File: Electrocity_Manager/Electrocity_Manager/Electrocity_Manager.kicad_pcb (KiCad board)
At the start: 2 copper layers, 100 x 77 mm, 193 parts, among them IC2 MAIN_SHUTDOWN, IC3 RELAY_STATE, IC4 ADC_RST, J1 SERIAL, P1 SWD, P10 EMERGENCY, P11 EMERGENCY, P12 FRAME_GRAND, P13 BATT_IN, P14 POWER_OUT, P15 FUN_OUT, P16 BATT_IN, P17 POWER_OUT, P18 FUN_OUT, P2 CAN, P3 CAN, P4 EMERGENCY_SIGNAL, P5 EMERGENCY_SIGNAL, P6 12V_OUT, P7 12V_OUT, P9 MAIN_SW, Q1 FET_N, Q2 NPN, Q3 NPN, Q4 NPN, Q5 NPN, Q6 NPN, Q7 FET_N, SW1 RST, U1 MAX3051, U10 BD9G101G, U11 ACS781, U12 V23134J1052D642, U13 ACS70331, U14 ACS781, U15 BD33FA1, U16 EC12PLRGBSDVBF, U17 LOGO, U18 LOGO, U19 MCP2221A, U2 STM32F405RG, U20 OSRB38C9AA, U21 OSRB38C9AA, U22 HSIN_946, U3 FULLCOLOR, U4 AQM0802_BL, U5 AP3211, U6 SI8900, U7 AZ1086H, U8 V23134J1052D642, U9 RPA60-12FW/P, X1 8MHz

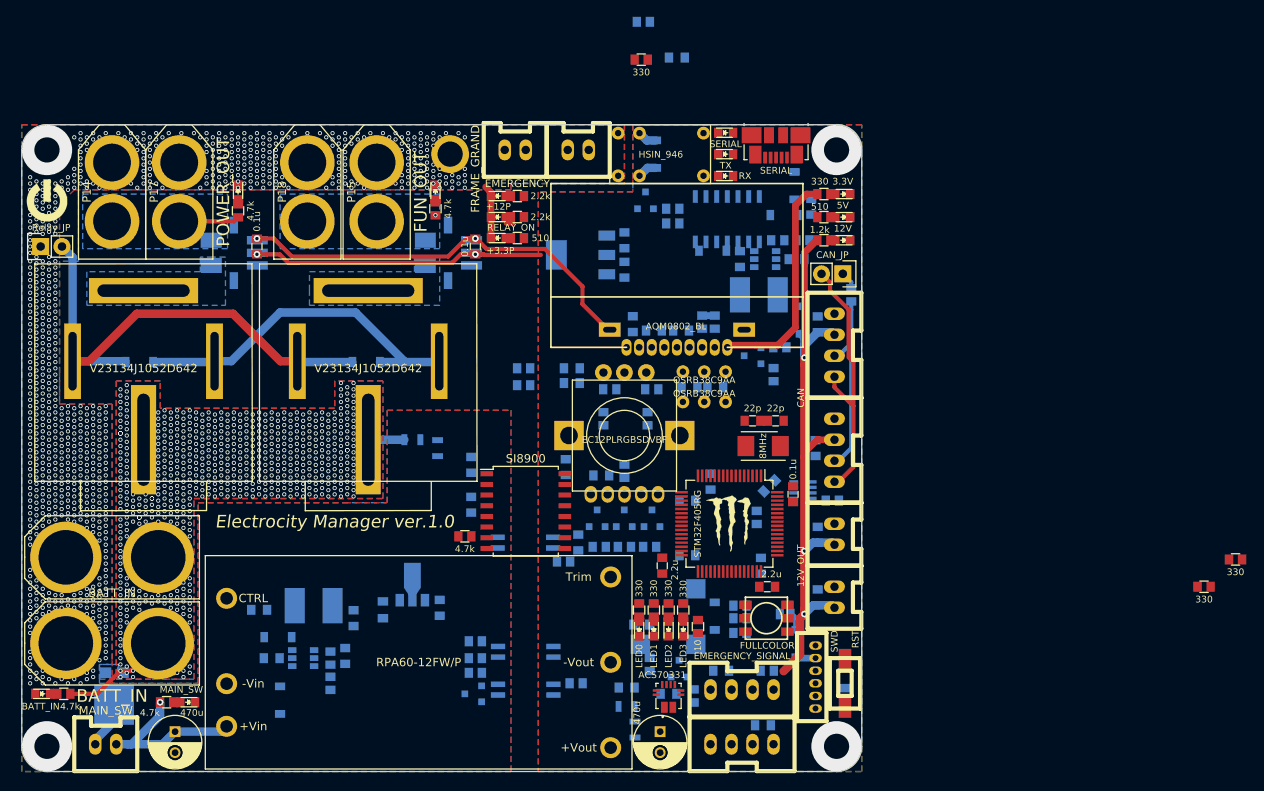
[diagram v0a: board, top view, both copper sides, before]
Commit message: 電源配線完了.フルカラーの秋月のエンコーダ基板面積的に使用できなかった...
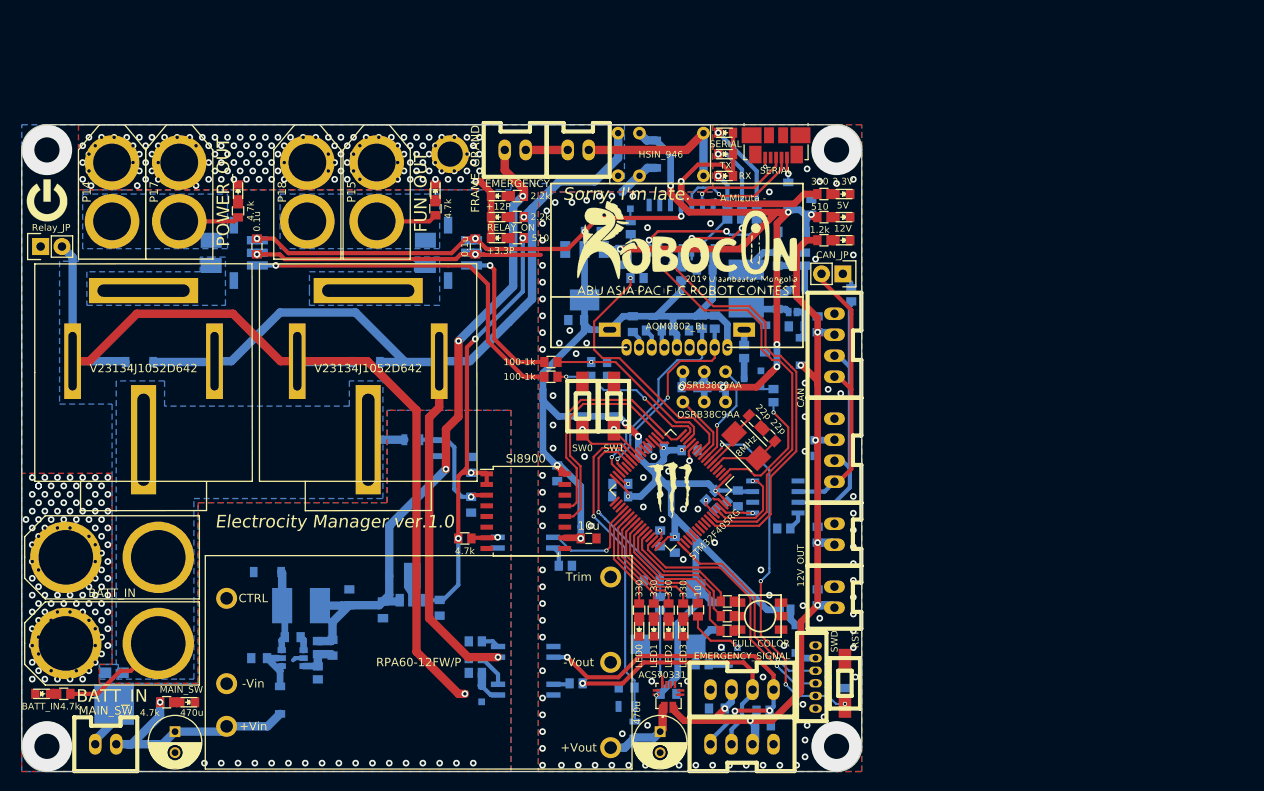
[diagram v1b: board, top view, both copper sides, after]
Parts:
- removed C45: 0.1u, Mizz_lib:C_0603
- removed Q4, Q5, Q6: NPN, Mizz_lib:SOT-123
- removed R49: 510, Mizz_lib:R_0603
- removed R50, R54, R55: 10k, Mizz_lib:R_0603
- removed R56, R57: 100, Mizz_lib:R_0603
- added C49: 10u, Mizz_lib:C_0603, B.Cu at (116.0, 110.8)
- added SW2: SW0, Mizz_lib:SW_SPST_CK_RS282G05A3, F.Cu at (114.8, 131.5)
- added SW3: SW1, Mizz_lib:SW_SPST_CK_RS282G05A3, F.Cu at (118.5, 131.5)
- added U23: LOGO, Mizz_lib:Battery_Killer_logo, B.Cu at (58.5, 154.5)
- C11, C13, C4, R19, R51, R58: moved to B.Cu
- C24, C26: value 22u -> 10u
- C28, R21, R40, R44: moved to F.Cu
- R1, R5: value 510 -> 330; moved to F.Cu
- R22, R23: value 330 -> 10k
- U1: footprint Package_TO_SOT_SMD:SOT-23-8 -> Mizz_lib:SOIC-8_3.9x4.9mm_Pitch1.27mm
- U16: value EC12PLRGBSDVBF -> LOGO; footprint Mizz_lib:EC12PLRGBSDVBF -> Mizz_lib:Robocon2019_30.0x30.0_silk
- U2: footprint Housings_QFP:TQFP-64_10x10mm_Pitch0.5mm -> Package_QFP:LQFP-64_10x10mm_P0.5mm
- U3: value FULLCOLOR -> FULL COLOR
- moved R19 73.2 mm to (132.0, 108.5), turned to 270 degrees
- moved R58 69.4 mm to (135.5, 108.5), turned to 270 degrees
- moved R59 30.3 mm to (126.5, 115.8), turned to 90 degrees
- moved R22 29.9 mm to (114.8, 133.5), turned to 270 degrees
- moved R23 29.2 mm to (118.5, 133.5), turned to 270 degrees
- moved C18 25.5 mm to (129.3, 115.2)
- moved U16 23.2 mm to (127.2, 113.0), turned to 0 degrees
- moved R51 21.8 mm to (133.8, 108.5), turned to 270 degrees
- moved R5 14.8 mm to (132.0, 156.5)
- moved C13 14.0 mm to (124.0, 147.2), turned to 270 degrees
- moved D11 12.2 mm to (136.5, 123.5), turned to 90 degrees
- moved R1 11.3 mm to (132.0, 154.8)
- moved C26 11.1 mm to (114.0, 121.2), turned to 180 degrees
- moved C11 11.0 mm to (119.2, 140.8), turned to 180 degrees
- moved C9 10.6 mm to (119.2, 142.2)
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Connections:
- C30 pad 1: +12C -> Net-(C30-Pad1)
- C30 pad 2: Net-(C30-Pad2) -> +12C
- C33 pad 1: /ADC12_IN4 -> /ADC12_IN1
- C39 pad 1: /ADC12_IN5 -> /ADC12_IN2
- C42 pad 1: /ADC12_IN6 -> /ADC12_IN9
- C44 pad 1: /ADC12_IN1 -> /ADC12_IN8
- IC3 pad 1: +12C -> /Coil
- IC4 pad 1: /PB2 -> /PB15
- Q2 pad 2: Net-(Q2-Pad2) -> GND
- Q2 pad 3: Net-(D9-Pad1) -> Net-(Q2-Pad3)
- Q3 pad 2: Net-(Q3-Pad2) -> GND
- R1 pad 1: GND -> /TIM1_CH4
- R1 pad 2: Net-(Q4-Pad2) -> Net-(R1-Pad2)
- R10 pad 1: /PB12 -> /PC6
- R13 pad 1: /PB13 -> /PC7
- R14 pad 1: /PB14 -> /PC8
- R16 pad 1: /PB15 -> /PC9
- R18 pad 2: Net-(Q7-Pad1) -> /PC2
- R21 pad 1: /TIM1_CH4 -> /TIM1_CH2
- R22 pad 1: /TIM1_CH3 -> +3.3V
- R22 pad 2: Net-(R22-Pad2) -> /PC5
- R23 pad 1: /TIM1_CH2 -> +3.3V
- R23 pad 2: Net-(R23-Pad2) -> /PC4
- R24 pad 1: GND -> Net-(Q2-Pad3)
- R24 pad 2: Net-(Q2-Pad2) -> Net-(D9-Pad1)
- R29 pad 1: GND -> Net-(Q3-Pad3)
- R29 pad 2: Net-(Q3-Pad2) -> Net-(R29-Pad2)
- R40 pad 1: /ADC12_IN4 -> /ADC12_IN1
- R41 pad 2: Net-(C30-Pad2) -> Net-(C30-Pad1)
- R42 pad 2: Net-(C30-Pad2) -> Net-(C30-Pad1)
- R44 pad 1: /ADC12_IN5 -> /ADC12_IN2
- R47 pad 1: /ADC12_IN6 -> /ADC12_IN9
- R48 pad 1: /PC15 -> /PC2
- R5 pad 1: GND -> /TIM1_CH3
- R5 pad 2: Net-(Q5-Pad2) -> Net-(R5-Pad2)
- R52 pad 1: /ADC12_IN1 -> /ADC12_IN8
- R53 pad 2: /ADC12_IN1 -> /ADC12_IN8
- U10 pad 3: Net-(C30-Pad2) -> Net-(C30-Pad1)
- U2 pad 14: Net-(U2-Pad14) -> /ADC12_IN2
- U2 pad 26: /PB0 -> /ADC12_IN8
- U2 pad 27: /PB1 -> /ADC12_IN9
- U2 pad 37: /TIM8_CH1 -> /PC6
- U2 pad 38: Net-(U2-Pad38) -> /PC7
- U2 pad 39: Net-(U2-Pad39) -> /PC8
- U2 pad 40: Net-(U2-Pad40) -> /PC9
- U3 pad 1: Net-(R21-Pad2) -> Net-(R1-Pad2)
- U3 pad 2: Net-(R22-Pad2) -> Net-(R5-Pad2)
- U3 pad 3: Net-(R23-Pad2) -> Net-(R21-Pad2)
- U4 pad 11: Net-(Q3-Pad3) -> Net-(R29-Pad2)
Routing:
- net +3.3V: track 77.6 -> 277.6 mm, vias 2 -> 16
- net +5V: track 2.32 -> 88.4 mm, vias 0 -> 8
- net /Coil: track 42.0 -> 125.2 mm, vias 0 -> 2
- net +12C: track 0.00 -> 78.2 mm, vias 0 -> 3
- net 3V3: track 0.00 -> 54.2 mm, vias 0 -> 4
- net /Relay_Out: track 58.6 -> 111.8 mm, vias 0 -> 1
- net /USART1_TX: track 0.00 -> 50.1 mm, vias 0 -> 1
- net /USART1_RX: track 0.00 -> 49.7 mm, vias 0 -> 1
- net /~NRST: track 0.00 -> 44.6 mm, vias 0 -> 4
- net Net-(R40-Pad2): track 0.00 -> 43.6 mm, vias 0 -> 1
- net /Relay_state: track 0.00 -> 42.9 mm, vias 0 -> 3
- net /ADC12_IN8: track 0.00 -> 39.3 mm, vias 0 -> 1
- net /PC2: track 0.00 -> 36.2 mm, vias 0 -> 1
- net /Fource_shutdown: track 0.00 -> 31.4 mm, vias 0 -> 1
- net /SWDIO: track 0.00 -> 31.1 mm, vias 0 -> 1
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- removed copper zone on F.Cu, net +BATT
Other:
- net class Default: clearance 0.2 -> 0.15
- rule trace_clearance: 0.2 -> 0.15
- board text added: ""Control power" can also be measured."
- board text added: "- A.Mizuta -"
- board text added: "Capable of measuring voltage and current of "Power supply"."
- board text added: "Designed by A.Mizuta in 2019/04/04."
- board text added: "Sorry, I'm late."
- board text added: "Specification:"
- board text removed: "Designed by A.Mizuta in 2019/03/22."

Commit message: 電源電圧電流監視電源基板
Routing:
- net GNDPWR: vias 257 -> 258
- net (no net): vias 5 -> 4
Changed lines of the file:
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@@
   )
   (setup
-    (last_trace_width 1)
+    (last_trace_width 0.25)
     (user_trace_width 0.3)
     (user_trace_width 0.5)
@@
   (via (at 145 172) (size 6) (drill 3) (layers F.Cu B.Cu) (net 0))
   (via (at 51 101) (size 6) (drill 3) (layers F.Cu B.Cu) (net 0))
-  (via (at 48.5 145) (size 0.8) (drill 0.4) (layers F.Cu B.Cu) (net 0))
   (via (at 131.28 160.2) (size 0.8) (drill 0.4) (layers F.Cu B.Cu) (net 1))
   (segment (start 102.990037 113.43) (end 103.050037 113.49) (width 0.5) (layer F.Cu) (net 1))
@@
   (via (at 69.75 174) (size 0.8) (drill 0.4) (layers F.Cu B.Cu) (net 14))
   (via (at 67.75 174) (size 0.8) (drill 0.4) (layers F.Cu B.Cu) (net 14))
+  (via (at 55.22 142.02) (size 0.8) (drill 0.4) (layers F.Cu B.Cu) (net 14))
   (segment (start 134.385 119.75) (end 136.5 121.865) (width 0.8) (layer B.Cu) (net 15))
   (segment (start 134.25 119.75) (end 134.385 119.75) (width 0.8) (layer B.Cu) (net 15))
@@
   (segment (start 122.69 111.73) (end 123.089999 111.330001) (width 0.3) (layer F.Cu) (net 140))
   (segment (start 131.9 110.69) (end 123.74 110.69) (width 0.3) (layer F.Cu) (net 140))
-  (segment (start 81.55048 162.44996) (end 83.08004 162.44996) (width 0.8) (layer B.Cu) (net 156))
   (segment (start 81.55048 159.35048) (end 81.2 159) (width 0.8) (layer B.Cu) (net 141))
   (segment (start 81.55048 160.55004) (end 81.55048 159.35048) (width 0.8) (layer B.Cu) (net 141))
@@
   (segment (start 116.08 144.62) (end 116.08 137.54) (width 0.25) (layer F.Cu) (net 154))
   (segment (start 119.17 136.48) (end 117.14 136.48) (width 0.25) (layer F.Cu) (net 154))
+  (segment (start 81.55048 162.44996) (end 83.08004 162.44996) (width 0.8) (layer B.Cu) (net 156))
   (segment (start 83.25 162.47) (end 83.25 161.03) (width 1) (layer B.Cu) (net 156))
   (segment (start 84.83 161.03) (end 85 161.2) (width 1) (layer B.Cu) (net 156))

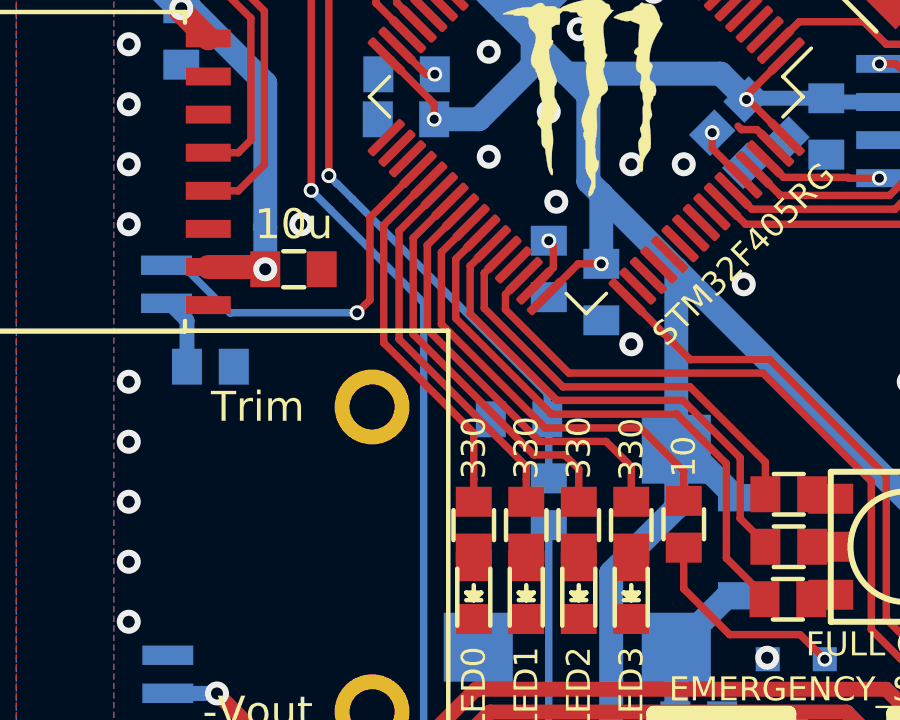
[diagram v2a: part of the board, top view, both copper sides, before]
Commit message: ブザとRC-LPFの抵抗が干渉してしまっていたため、配置を変えた
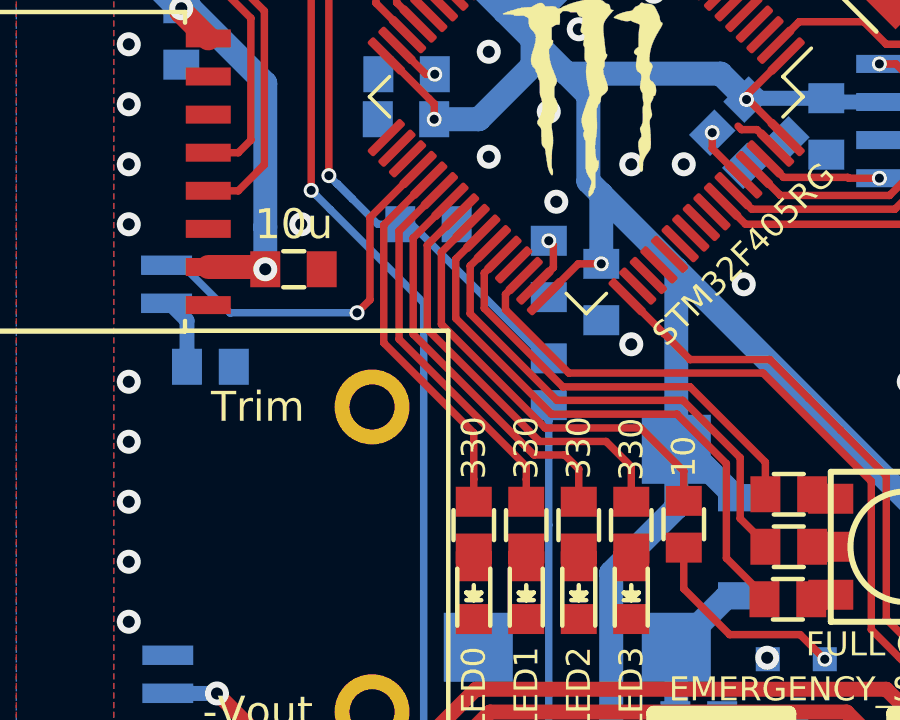
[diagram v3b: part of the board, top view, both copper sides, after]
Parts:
- C37, C43: value 22u -> 1u
- moved C42 7.16 mm to (120.0, 145.8), turned to 0 degrees
- moved R47 4.00 mm to (124.0, 151.0)
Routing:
- net Net-(R47-Pad2): track 9.68 -> 13.8 mm
- net /ADC12_IN9: track 24.2 -> 21.6 mm
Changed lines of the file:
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@@
     (thickness 1.6)
     (drawings 36)
-    (tracks 1367)
+    (tracks 1370)
     (zones 0)
     (modules 187)
@@
       (effects (font (size 1 1) (thickness 0.15)) (justify mirror))
     )
-    (fp_text value 2.2u (at 2.899138 0 270) (layer B.SilkS)
+    (fp_text value 2.2u (at -3 0 270) (layer B.SilkS)
       (effects (font (size 0.8 0.8) (thickness 0.15)) (justify mirror))
     )
@@
   )
   (module Mizz_lib:C_0603 (layer B.Cu)
-    (at 123 152.25 180)
+    (at 120 145.75)
     (descr "Capacitor SMD 0603, reflow soldering, AVX (see smccp.pdf)")
     (tags "capacitor 0603")
     (attr smd)
-    (fp_text reference C42 (at 0 1.9 180) (layer B.SilkS) hide
+    (fp_text reference C42 (at 0 1.9) (layer B.SilkS) hide
       (effects (font (size 1 1) (thickness 0.15)) (justify mirror))
     )
-    (fp_text value 1u (at 2.5 0 180) (layer B.SilkS)
+    (fp_text value 1u (at 0 -1.25) (layer B.SilkS)
       (effects (font (size 0.8 0.8) (thickness 0.15)) (justify mirror))
     )
@@
     (fp_line (start -0.35 0.6) (end 0.35 0.6) (layer B.SilkS) (width 0.15))
     (fp_line (start 0.35 -0.6) (end -0.35 -0.6) (layer B.SilkS) (width 0.15))
-    (pad 1 smd rect (at -0.95 0 180) (size 1 1.2) (layers B.Cu B.Paste B.Mask)
+    (pad 1 smd rect (at -0.95 0) (size 1 1.2) (layers B.Cu B.Paste B.Mask)
       (net 153 /ADC12_IN9))
-    (pad 2 smd rect (at 0.93 0 180) (size 1 1.2) (layers B.Cu B.Paste B.Mask)
+    (pad 2 smd rect (at 0.93 0) (size 1 1.2) (layers B.Cu B.Paste B.Mask)
       (net 1 GND))
     (model C:/Users/Mizuta/Downloads/kicad-packages3D-master/Capacitor_SMD.3dshapes/C_0603_1608Metric.step
@@
       (effects (font (size 1 1) (thickness 0.15)) (justify mirror))
     )
-    (fp_text value 22u (at 0 1.5 90) (layer B.SilkS)
+    (fp_text value 1u (at 0 1.5 90) (layer B.SilkS)
       (effects (font (size 0.8 0.8) (thickness 0.15)) (justify mirror))
     )
@@
       (effects (font (size 1 1) (thickness 0.15)) (justify mirror))
     )
-    (fp_text value NPN (at -2.25 -1.25 270) (layer B.SilkS)
+    (fp_text value NPN (at 0.25 -2.25) (layer B.SilkS)
       (effects (font (size 1 1) (thickness 0.15)) (justify mirror))
     )
@@
   )
   (module Mizz_lib:R_0603 (layer B.Cu)
-    (at 124 155 270)
+    (at 124 151 270)
     (descr "Resistor SMD 0603, reflow soldering, Vishay (see dcrcw.pdf)")
     (tags "resistor 0603")
@@
       (effects (font (size 1 1) (thickness 0.15)) (justify mirror))
     )
-    (fp_text value 100-1k (at 0 -1.5 270) (layer B.SilkS)
+    (fp_text value 100-1k (at -0.5 1.25 90) (layer B.SilkS)
       (effects (font (size 0.8 0.8) (thickness 0.15)) (justify mirror))
     )
@@
       (effects (font (size 1 1) (thickness 0.15)) (justify mirror))
     )
-    (fp_text value 22u (at -3 0 90) (layer B.SilkS)
+    (fp_text value 1u (at -3 0 90) (layer B.SilkS)
       (effects (font (size 0.8 0.8) (thickness 0.2)) (justify mirror))
     )
@@
   (segment (start 124.25 164.65) (end 124.25 163.72) (width 0.25) (layer F.Cu) (net 84))
   (segment (start 124 155.78) (end 124 163.47) (width 0.25) (layer B.Cu) (net 84))
+  (segment (start 124 152.3) (end 123.95 152.25) (width 0.25) (layer B.Cu) (net 84))
+  (segment (start 124 155.78) (end 124 151.78) (width 0.25) (layer B.Cu) (net 84))
   (via (at 135.02 144.215) (size 0.5) (drill 0.3) (layers F.Cu B.Cu) (net 85))
   (segment (start 131.826093 144.187005) (end 131.207375 143.568287) (width 0.25) (layer F.Cu) (net 85))
@@
   (segment (start 126.75 153.83) (end 126.75 155) (width 0.25) (layer F.Cu) (net 152))
   (segment (start 125.91 152.99) (end 126.75 153.83) (width 0.25) (layer F.Cu) (net 152))
-  (segment (start 124 152.3) (end 123.95 152.25) (width 0.25) (layer B.Cu) (net 153))
-  (segment (start 124 154.22) (end 124 152.3) (width 0.25) (layer B.Cu) (net 153))
-  (segment (start 123.95 152.25) (end 123.95 151.4) (width 0.25) (layer B.Cu) (net 153))
   (segment (start 117.46 144.91) (end 117.45 144.91) (width 0.25) (layer B.Cu) (net 153))
-  (segment (start 123.95 151.4) (end 117.46 144.91) (width 0.25) (layer B.Cu) (net 153))
   (segment (start 119.734568 137.752334) (end 119.732334 137.752334) (width 0.25) (layer F.Cu) (net 153))
   (segment (start 120.353286 138.371052) (end 119.734568 137.752334) (width 0.25) (layer F.Cu) (net 153))
@@
   (segment (start 116.67 137.67) (end 116.67 144.13) (width 0.25) (layer F.Cu) (net 153))
   (segment (start 117.46 144.91) (end 116.95 144.4) (width 0.25) (layer B.Cu) (net 153))
-  (segment (start 116.94 144.4) (end 116.95 144.4) (width 0.25) (layer B.Cu) (net 153))
   (segment (start 116.67 144.13) (end 116.94 144.4) (width 0.25) (layer B.Cu) (net 153))
+  (segment (start 119.43 145.75) (end 119.05 145.75) (width 0.25) (layer B.Cu) (net 153))
+  (segment (start 123.9 150.22) (end 119.43 145.75) (width 0.25) (layer B.Cu) (net 153))
+  (segment (start 124 150.22) (end 123.9 150.22) (width 0.25) (layer B.Cu) (net 153))
+  (segment (start 116.95 144.4) (end 116.94 144.4) (width 0.25) (layer B.Cu) (net 153))
+  (segment (start 118.3 145.75) (end 116.95 144.4) (width 0.25) (layer B.Cu) (net 153))
+  (segment (start 119.05 145.75) (end 118.3 145.75) (width 0.25) (layer B.Cu) (net 153))
   (segment (start 121 167.3) (end 120.95 167.25) (width 0.25) (layer B.Cu) (net 154))
   (segment (start 121 169.05) (end 121 167.3) (width 0.25) (layer B.Cu) (net 154))

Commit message: 緑ピカチュウか何か
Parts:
- added U24: LOGO, Mizz_lib:Pikatyuu_15x15, B.Cu at (93.0, 164.0)
- added U25: LOGO, Mizz_lib:MonsterBall_10x10_silk, B.Cu at (83.5, 169.2)
- added U26: LOGO, Mizz_lib:PiOtyu_silk_21.3x6.8, B.Cu at (110.0, 155.5)
- C32: value 470u -> 220u
- C35: value 470u -> 100u
- U9: value RPA60-12FW/P -> RPA60-12FW/N
- moved D14 1.00 mm to (50.5, 166.8)
- moved R33 1.00 mm to (53.0, 166.8)
- moved R46 1.00 mm to (98.5, 136.5)
- moved D15 0.50 mm to (67.8, 167.2)
- moved P16 0.50 mm to (58.8, 150.0)
- moved R34 0.50 mm to (65.2, 167.2)
- moved P13 0.25 mm to (58.8, 160.0)
- moved U12 0.25 mm to (89.2, 127.2)
- moved U8 0.25 mm to (62.5, 127.2)
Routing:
- net /24V: track 27.9 -> 27.4 mm
- net GNDPWR: vias 258 -> 245
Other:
- board text added: "Electrocity Manager ver.1.1"
- board text added: "Pocket Monster "Pikachu""
- board text removed: "Electrocity Manager ver.1.0"
